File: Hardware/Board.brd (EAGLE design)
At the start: 100 x 80 mm, 55 parts, among them U1 EDISON_CONNECTOR_FULLMOUNTING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, U2 LAN9512-JZX, U4 EDISON_CONNECTOR_FULLHEADER, X1 J1011F01P

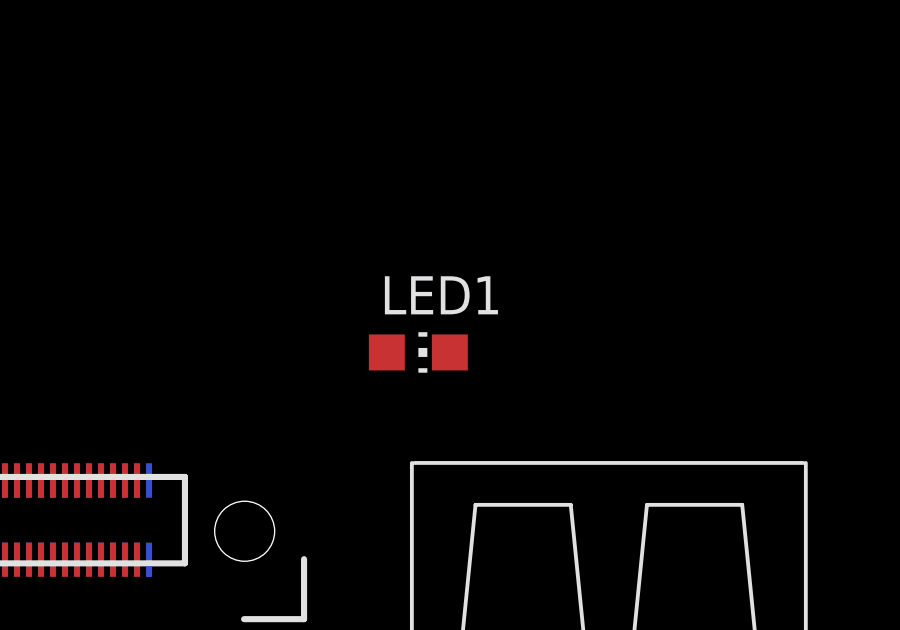
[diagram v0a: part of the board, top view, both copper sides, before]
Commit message: Changed LED from 0805 package to 0603 package
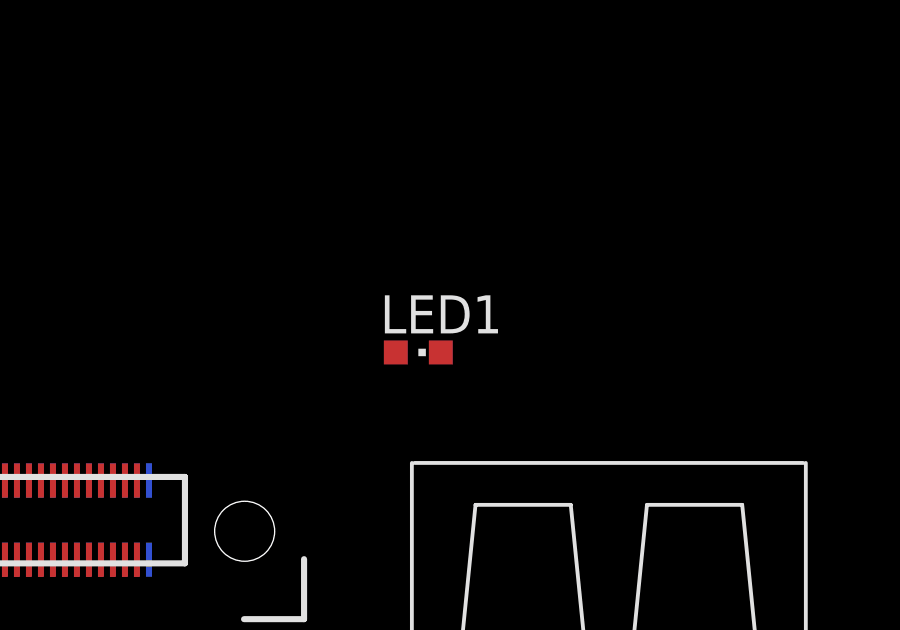
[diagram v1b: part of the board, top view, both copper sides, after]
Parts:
- LED1: device led:CHIP-LED0805 -> led:CHIPLED_0603
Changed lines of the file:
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@@
 <element name="L1" library="murata-inductors" package="L0603" value="2.0A 120Ohm" x="62.23" y="60.96" rot="R270"/>
 <element name="L2" library="murata-inductors" package="L0603" value="2.0A 120Ohm" x="71.12" y="13.97" rot="R270"/>
-<element name="LED1" library="led" package="CHIP-LED0805" value="Green LED" x="41.91" y="62.23" rot="R270"/>
+<element name="LED1" library="led" package="CHIPLED_0603" value="Green LED" x="41.91" y="62.23" rot="R270"/>
 <element name="R1" library="resistor" package="R0603" value="10K" x="76.2" y="41.91" rot="R270"/>
 <element name="R10" library="resistor" package="R1210" value="0" x="63.5" y="33.02" rot="R270"/>
@@
 <contactref element="LED1" pad="C"/>
 <contactref element="U2" pad="20"/>
-<wire x1="45.1358" y1="18.7706" x2="42.96" y2="62.23" width="0" layer="19" extent="1-1"/>
+<wire x1="45.1358" y1="18.7706" x2="42.66" y2="62.23" width="0" layer="19" extent="1-1"/>
 </signal>
 <signal name="N$20">
 <contactref element="LED1" pad="A"/>
 <contactref element="R13" pad="2"/>
-<wire x1="40.86" y1="62.23" x2="76.2" y2="31.1" width="0" layer="19" extent="1-1"/>
+<wire x1="41.16" y1="62.23" x2="76.2" y2="31.1" width="0" layer="19" extent="1-1"/>
 </signal>
 <signal name="N$21">

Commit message: Rolled back previous change
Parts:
- LED1: device led:CHIPLED_0603 -> led:CHIP-LED0805
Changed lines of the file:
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@@
 <element name="L1" library="murata-inductors" package="L0603" value="2.0A 120Ohm" x="62.23" y="60.96" rot="R270"/>
 <element name="L2" library="murata-inductors" package="L0603" value="2.0A 120Ohm" x="71.12" y="13.97" rot="R270"/>
-<element name="LED1" library="led" package="CHIPLED_0603" value="Green LED" x="41.91" y="62.23" rot="R270"/>
+<element name="LED1" library="led" package="CHIP-LED0805" value="Green LED" x="41.91" y="62.23" rot="R270"/>
 <element name="R1" library="resistor" package="R0603" value="10K" x="76.2" y="41.91" rot="R270"/>
 <element name="R10" library="resistor" package="R1210" value="0" x="63.5" y="33.02" rot="R270"/>
@@
 <contactref element="LED1" pad="C"/>
 <contactref element="U2" pad="20"/>
-<wire x1="45.1358" y1="18.7706" x2="42.66" y2="62.23" width="0" layer="19" extent="1-1"/>
+<wire x1="45.1358" y1="18.7706" x2="42.96" y2="62.23" width="0" layer="19" extent="1-1"/>
 </signal>
 <signal name="N$20">
 <contactref element="LED1" pad="A"/>
 <contactref element="R13" pad="2"/>
-<wire x1="41.16" y1="62.23" x2="76.2" y2="31.1" width="0" layer="19" extent="1-1"/>
+<wire x1="40.86" y1="62.23" x2="76.2" y2="31.1" width="0" layer="19" extent="1-1"/>
 </signal>
 <signal name="N$21">
